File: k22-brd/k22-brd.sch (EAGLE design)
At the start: 34 parts, among them J1 61302011121, J2 61302011121, J3 CORTEX_DEBUG_PTH

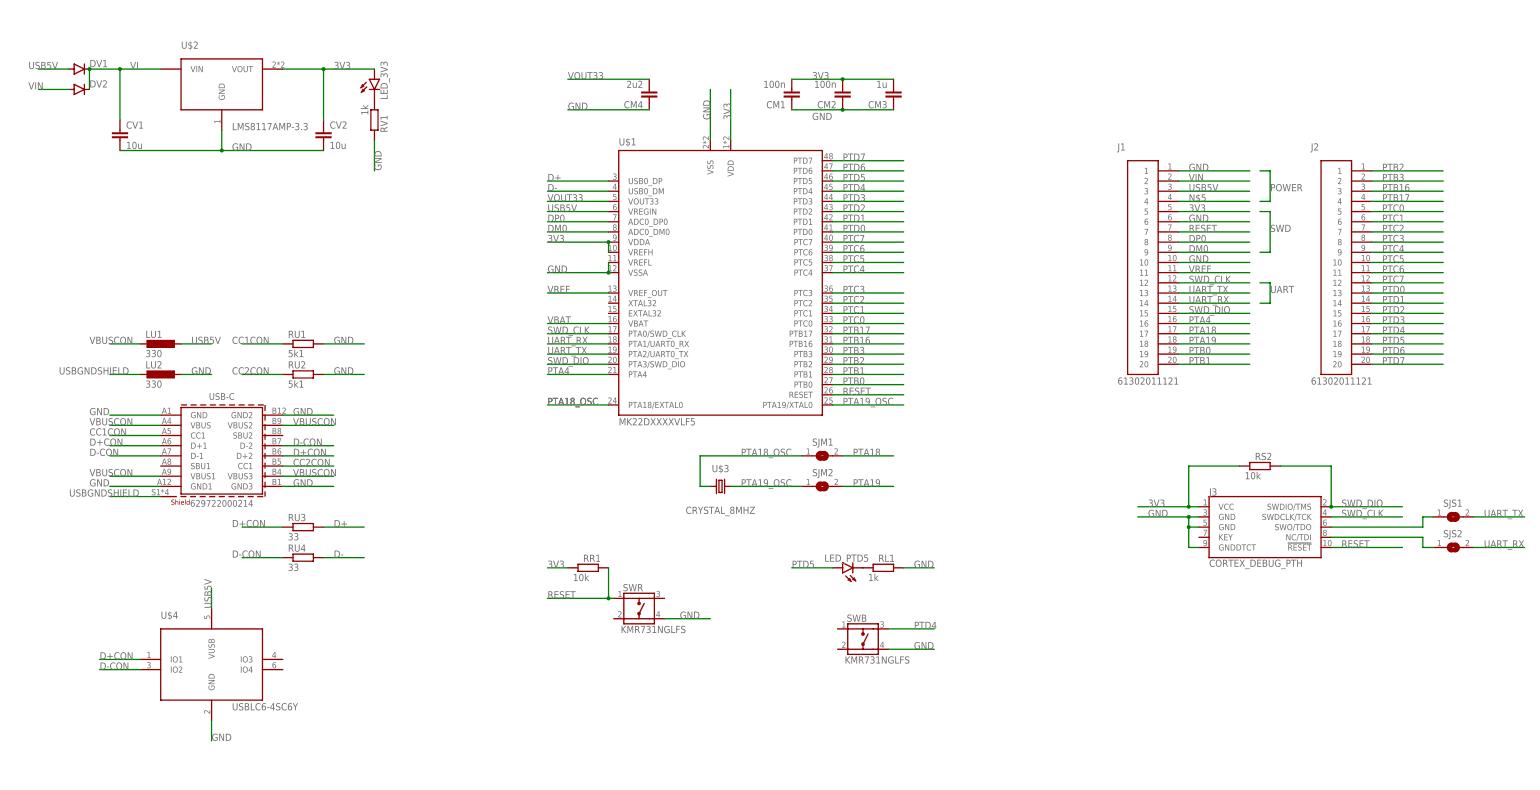
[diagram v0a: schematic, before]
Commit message: Different pin order on headers
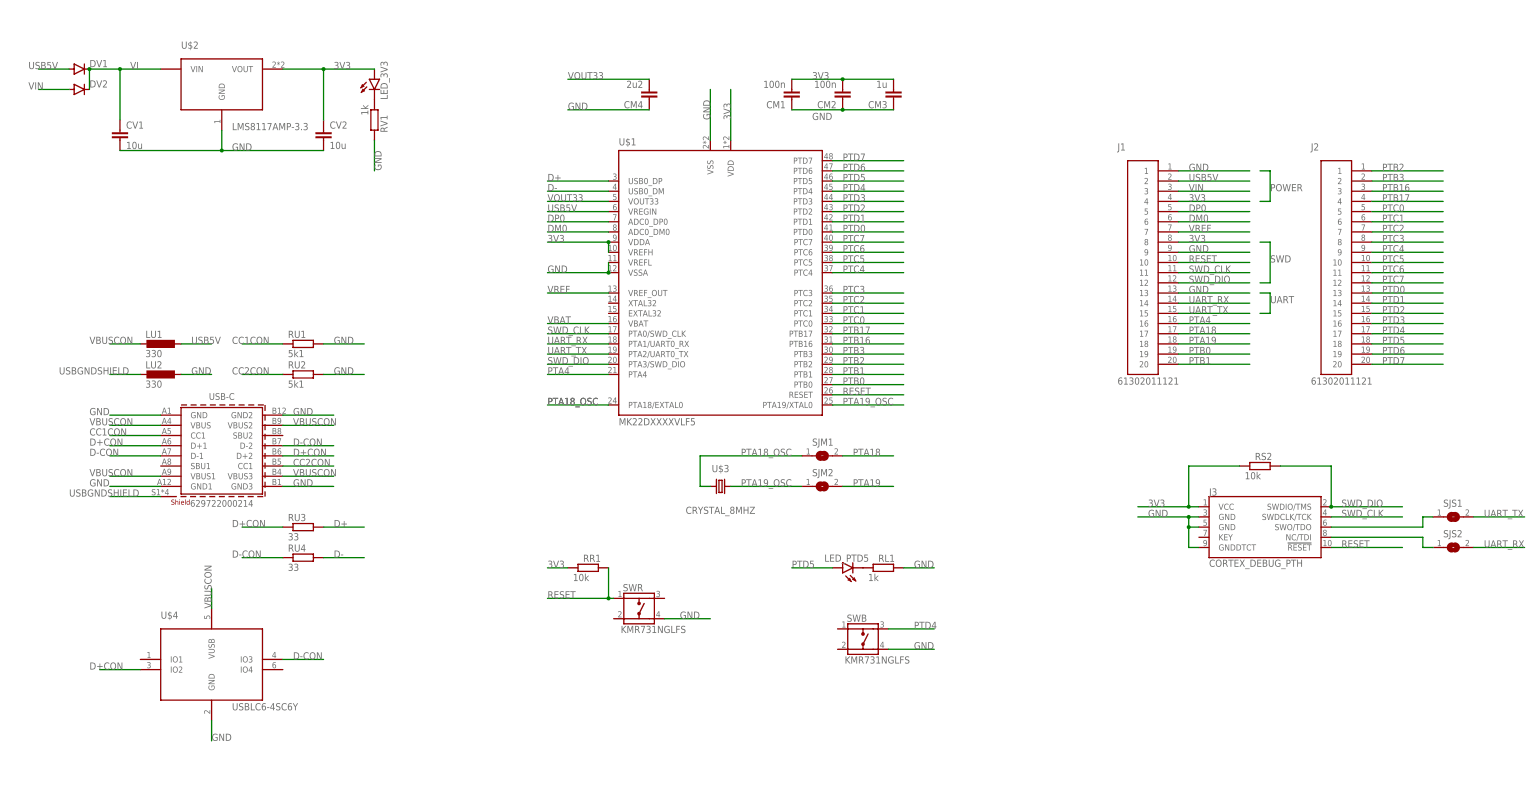
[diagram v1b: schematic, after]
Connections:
- removed net N$5: J1.4
- net 3V3: now also J1.4, J1.8; no longer J1.5
- net D+CON: now also U$4.IO2; no longer U$4.IO1
- net D-CON: now also U$4.IO3; no longer U$4.IO2
- net DM0: now also J1.6; no longer J1.9
- net DP0: now also J1.5; no longer J1.8
- net GND: now also J1.13, J1.9; no longer J1.10, J1.6
- net RESET: now also J1.10; no longer J1.7
- net SWD_CLK: now also J1.11; no longer J1.12
- net SWD_DIO: now also J1.12; no longer J1.15
- net UART_TX: now also J1.15; no longer J1.13
- net USB5V: now also J1.2; no longer J1.3, U$4.VUSB
- net VBUSCON: now also U$4.VUSB
- net VIN: now also J1.3; no longer J1.2
- net VREF: now also J1.7; no longer J1.11

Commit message: prezehleno
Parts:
- removed U$4: USBLC6-4SC6Y, vym0038_k22_misc:USBLC6-4SC6Y
- added CU1: <1,10>u, rcl:C-EUC0805
- added U$5: USBLC6-2SC6, vym0038_k22_misc:USBLC6-2SC6
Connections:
- net D+CON: now also U$5.IO2; no longer U$4.IO2
- net D-CON: now also U$5.IO1; no longer U$4.IO3
- net GND: now also CU1.1, U$5.GND; no longer U$4.GND
- net USB5V: now also CU1.2, J1.3; no longer J1.2
- net VBUSCON: now also U$5.VUSB; no longer U$4.VUSB
- net VIN: now also J1.2; no longer J1.3
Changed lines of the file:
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@@
 <part name="LED_3V3" library="led" library_urn="urn:adsk.eagle:library:259" deviceset="LED" device="CHIP-LED0805" package3d_urn="urn:adsk.eagle:package:15818/2"/>
 <part name="U$2" library="vym0038_k22_misc" deviceset="LMS8117AMP-3.3" device=""/>
-<part name="U$4" library="vym0038_k22_misc" deviceset="USBLC6-4SC6Y" device=""/>
+<part name="U$5" library="vym0038_k22_misc" deviceset="USBLC6-2SC6" device=""/>
+<part name="CU1" library="rcl" library_urn="urn:adsk.eagle:library:334" deviceset="C-EU" device="C0805" package3d_urn="urn:adsk.eagle:package:23617/2" value="&lt;1,10&gt;u"/>
 </parts>
 <sheets>
@@
 <text x="-66.04" y="127" size="1.778" layer="104">V Voltage Regulator</text>
 <text x="63.5" y="127" size="1.778" layer="104">M MCU</text>
-<text x="-50.8" y="60.96" size="1.778" layer="104">U USB Connector</text>
+<text x="-50.8" y="68.58" size="1.778" layer="104">U USB Connector</text>
 <text x="124.46" y="2.54" size="1.778" layer="104">L LED PTD5</text>
 <text x="63.5" y="2.54" size="1.778" layer="104">R RESET</text>
@@
 <attribute name="VALUE" x="-15.24" y="104.14" size="1.778" layer="96"/>
 </instance>
-<instance part="U$4" gate="G$1" x="-20.32" y="-30.48" smashed="yes">
-<attribute name="NAME" x="-33.02" y="-17.78" size="1.778" layer="95"/>
-<attribute name="VALUE" x="-15.24" y="-40.64" size="1.778" layer="96"/>
+<instance part="U$5" gate="G$1" x="-15.24" y="-35.56" smashed="yes">
+<attribute name="NAME" x="-27.94" y="-22.86" size="1.778" layer="95"/>
+<attribute name="VALUE" x="-10.16" y="-45.72" size="1.778" layer="96"/>
+</instance>
+<instance part="CU1" gate="G$1" x="-33.02" y="58.42" smashed="yes" rot="R90">
+<attribute name="NAME" x="-33.401" y="59.944" size="1.778" layer="95" rot="R90"/>
+<attribute name="VALUE" x="-28.321" y="59.944" size="1.778" layer="96" rot="R90"/>
 </instance>
 </instances>
@@
 </segment>
 <segment>
-<wire x1="-20.32" y1="-43.18" x2="-20.32" y2="-48.26" width="0.1524" layer="91"/>
-<label x="-20.32" y="-48.26" size="1.778" layer="95"/>
-<pinref part="U$4" gate="G$1" pin="GND"/>
-</segment>
-<segment>
 <pinref part="SWB" gate="G$1" pin="4"/>
 <wire x1="148.59" y1="-25.4" x2="160.02" y2="-25.4" width="0.1524" layer="91"/>
@@
 <pinref part="J1" gate="G$1" pin="9"/>
 </segment>
+<segment>
+<wire x1="-15.24" y1="-48.26" x2="-15.24" y2="-53.34" width="0.1524" layer="91"/>
+<pinref part="U$5" gate="G$1" pin="GND"/>
+<label x="-15.24" y="-55.88" size="1.778" layer="95" rot="R90"/>
+</segment>
+<segment>
+<wire x1="-45.72" y1="58.42" x2="-35.56" y2="58.42" width="0.1524" layer="91"/>
+<pinref part="CU1" gate="G$1" pin="1"/>
+<label x="-45.72" y="58.42" size="1.778" layer="95"/>
+</segment>
 </net>
 <net name="VBUSCON" class="0">
@@
 </segment>
 <segment>
-<wire x1="-20.32" y1="-10.16" x2="-20.32" y2="-15.24" width="0.1524" layer="91"/>
-<label x="-20.32" y="-15.24" size="1.778" layer="95" rot="R90"/>
-<pinref part="U$4" gate="G$1" pin="VUSB"/>
+<wire x1="-15.24" y1="-15.24" x2="-15.24" y2="-20.32" width="0.1524" layer="91"/>
+<pinref part="U$5" gate="G$1" pin="VUSB"/>
+<label x="-15.24" y="-20.32" size="1.778" layer="95" rot="R90"/>
 </segment>
 </net>
@@
 </segment>
 <segment>
-<pinref part="U$4" gate="G$1" pin="IO2"/>
-<wire x1="-38.1" y1="-30.48" x2="-48.26" y2="-30.48" width="0.1524" layer="91"/>
-<label x="-50.8" y="-30.48" size="1.778" layer="95"/>
+<wire x1="17.78" y1="-33.02" x2="2.54" y2="-33.02" width="0.1524" layer="91"/>
+<pinref part="U$5" gate="G$1" pin="IO2"/>
+<label x="10.16" y="-33.02" size="1.778" layer="95"/>
 </segment>
 </net>
@@
 </segment>
 <segment>
-<pinref part="U$4" gate="G$1" pin="IO3"/>
-<wire x1="-2.54" y1="-27.94" x2="7.62" y2="-27.94" width="0.1524" layer="91"/>
-<label x="0" y="-27.94" size="1.778" layer="95"/>
+<wire x1="-43.18" y1="-33.02" x2="-33.02" y2="-33.02" width="0.1524" layer="91"/>
+<pinref part="U$5" gate="G$1" pin="IO1"/>
+<label x="-43.18" y="-33.02" size="1.778" layer="95"/>
 </segment>
 </net>
@@
 <wire x1="-27.94" y1="50.8" x2="-20.32" y2="50.8" width="0.1524" layer="91"/>
 <label x="-25.4" y="50.8" size="1.778" layer="95"/>
+<pinref part="CU1" gate="G$1" pin="2"/>
+<wire x1="-27.94" y1="50.8" x2="-27.94" y2="58.42" width="0.1524" layer="91"/>
+<junction x="-27.94" y="50.8"/>
 </segment>
 <segment>
@@
 </segment>
 <segment>
-<wire x1="220.98" y1="91.44" x2="238.76" y2="91.44" width="0.1524" layer="91"/>
-<label x="223.52" y="91.44" size="1.778" layer="95"/>
-<pinref part="J1" gate="G$1" pin="2"/>
+<wire x1="220.98" y1="88.9" x2="238.76" y2="88.9" width="0.1524" layer="91"/>
+<label x="223.52" y="88.9" size="1.778" layer="95"/>
+<pinref part="J1" gate="G$1" pin="3"/>
 </segment>
 </net>
@@
 </segment>
 <segment>
-<wire x1="220.98" y1="88.9" x2="238.76" y2="88.9" width="0.1524" layer="91"/>
-<label x="223.52" y="88.9" size="1.778" layer="95"/>
-<pinref part="J1" gate="G$1" pin="3"/>
-</segment>
-</net>
+<wire x1="220.98" y1="91.44" x2="238.76" y2="91.44" width="0.1524" layer="91"/>
+<label x="223.52" y="91.44" size="1.778" layer="95"/>
+<pinref part="J1" gate="G$1" pin="2"/>
+</segment>
+</net>

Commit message: uprava routovani D+/-
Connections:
- net D+CON: now also U$5.IO1; no longer U$5.IO2
- net D-CON: now also U$5.IO2; no longer U$5.IO1
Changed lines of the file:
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@@
 </segment>
 <segment>
-<wire x1="17.78" y1="-33.02" x2="2.54" y2="-33.02" width="0.1524" layer="91"/>
-<pinref part="U$5" gate="G$1" pin="IO2"/>
-<label x="10.16" y="-33.02" size="1.778" layer="95"/>
+<wire x1="-43.18" y1="-33.02" x2="-33.02" y2="-33.02" width="0.1524" layer="91"/>
+<pinref part="U$5" gate="G$1" pin="IO1"/>
+<label x="-43.18" y="-33.02" size="1.778" layer="95"/>
 </segment>
 </net>
@@
 </segment>
 <segment>
-<wire x1="-43.18" y1="-33.02" x2="-33.02" y2="-33.02" width="0.1524" layer="91"/>
-<pinref part="U$5" gate="G$1" pin="IO1"/>
-<label x="-43.18" y="-33.02" size="1.778" layer="95"/>
+<wire x1="17.78" y1="-33.02" x2="2.54" y2="-33.02" width="0.1524" layer="91"/>
+<pinref part="U$5" gate="G$1" pin="IO2"/>
+<label x="10.16" y="-33.02" size="1.778" layer="95"/>
 </segment>
 </net>

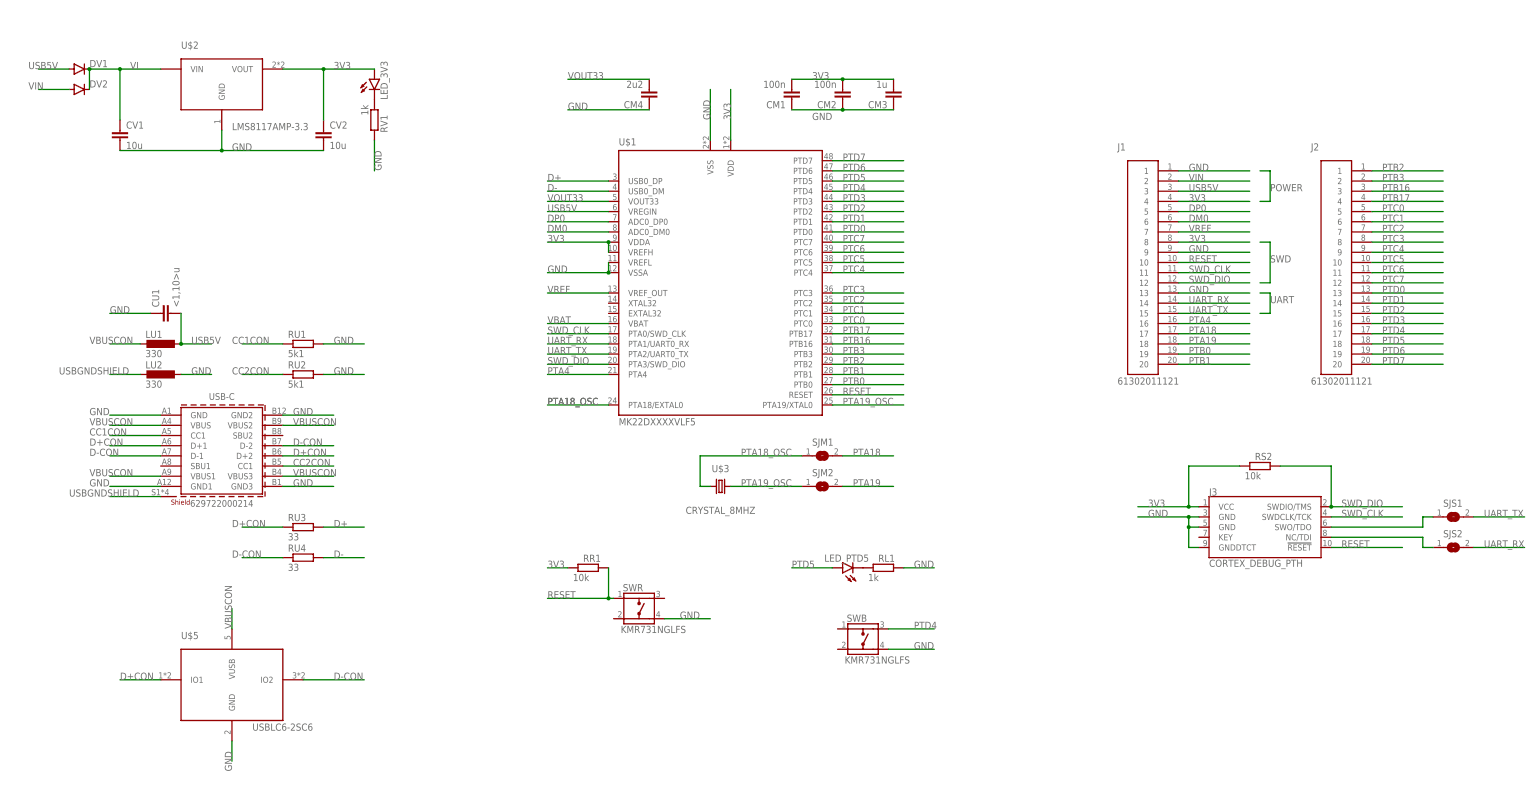
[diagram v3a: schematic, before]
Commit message: Pridany ramecky do schematu
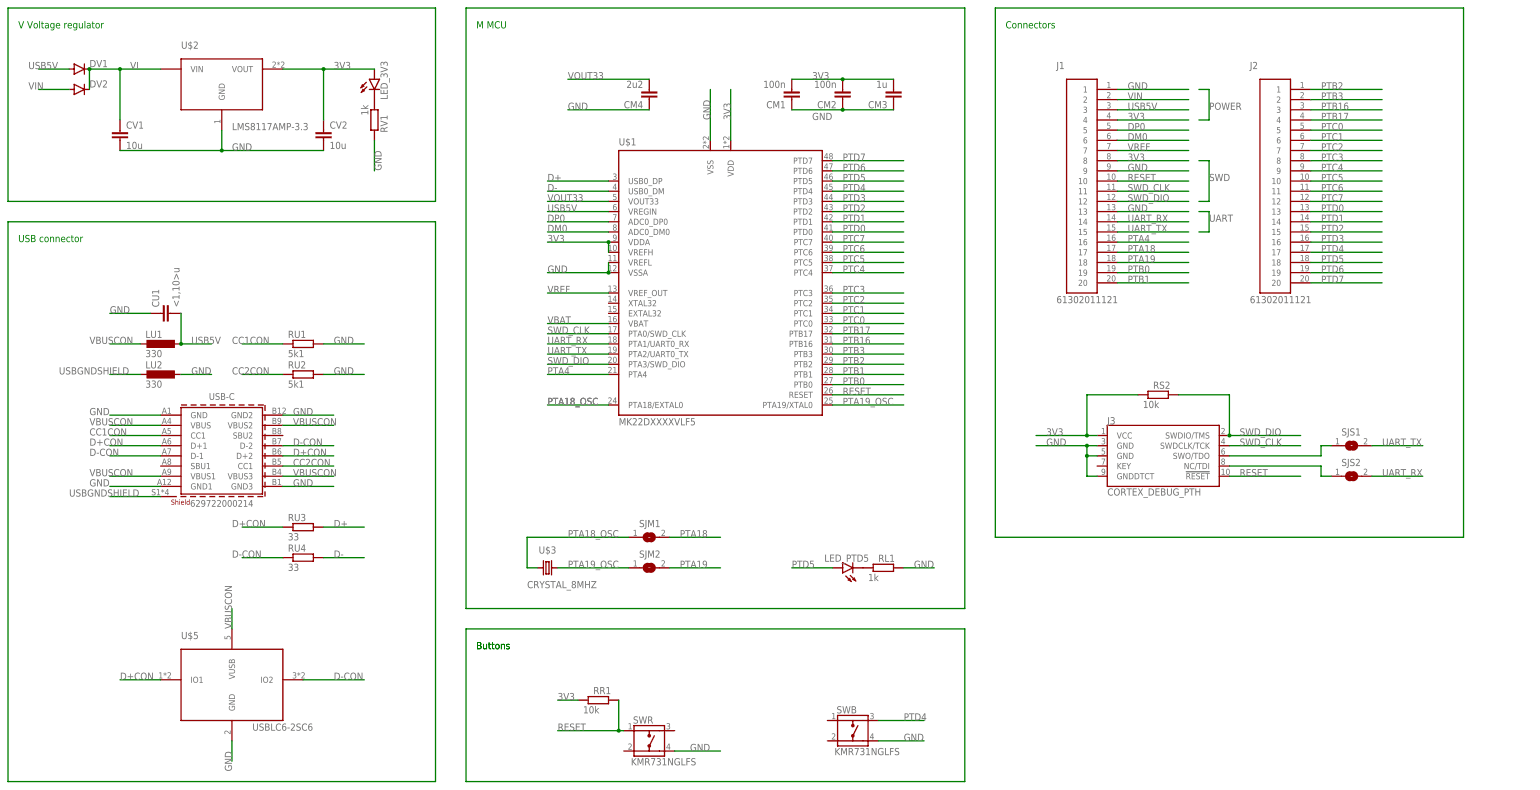
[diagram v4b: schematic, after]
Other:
- note added: "Buttons"
- note added: "Connectors"
- note added: "USB connector"
- note added: "V Voltage regulator"
- note removed: "U USB Connector"
- note removed: "V Voltage Regulator"
- moved on the sheet: J1, J2, J3, RR1, RS2, SJM1, SJM2, SJS1, SJS2, SWB, SWR, U$3

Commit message: Modre ramecky
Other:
- note added: "PTD4 BTN"
- note added: "PTD5 LED"
- note added: "Reset BTN"
- note removed: "B BUTTON PTD4"
- note removed: "Buttons"
- note removed: "L LED PTD5"
- note removed: "R RESET"
- moved on the sheet: LED_PTD5, RL1, RR1, SWB, SWR, U$5
